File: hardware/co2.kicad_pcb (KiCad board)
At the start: 2 copper layers, 25 x 35 mm, 24 parts, among them P1 CON-SENSOR, U1 M24C64, U2 TLV271, U3 MSH-Sensor, U4 DRILL, U5 DRILL, U6 DRILL, U7 DRILL

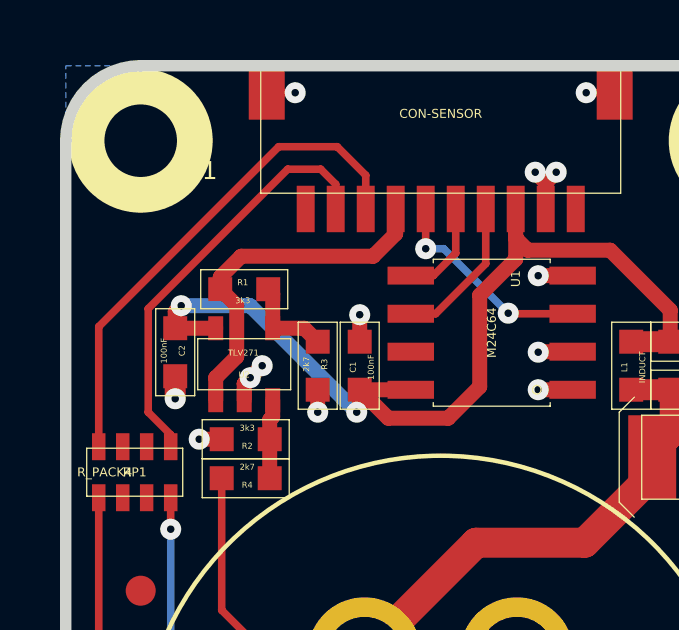
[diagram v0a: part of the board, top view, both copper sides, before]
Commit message: add configurable pin for co2 sensor config
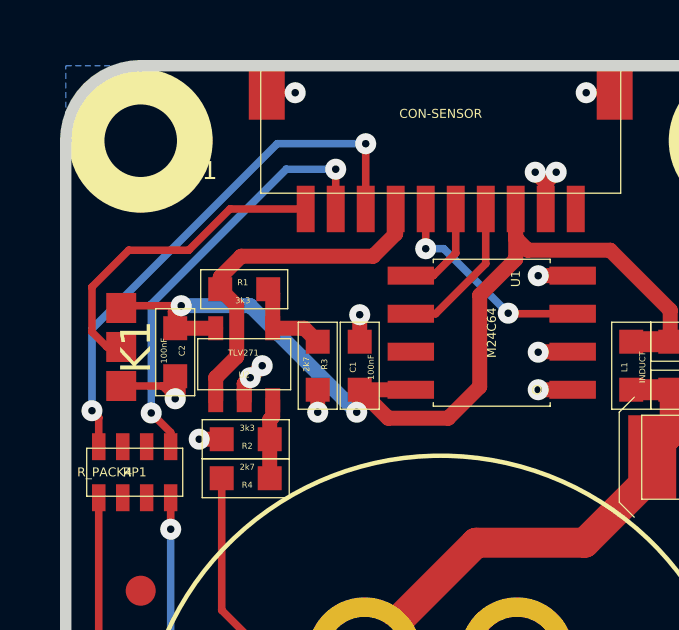
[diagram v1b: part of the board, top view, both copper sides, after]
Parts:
- added K1: CONN_3, kicad-libraries:con-conf, F.Cu at (133.2, 77.5)
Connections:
- P1 pad 10: (no net) -> Net-(K1-Pad2)
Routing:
- net Net-(K1-Pad2): track 0.00 -> 10.9 mm
- net 3V3: track 31.8 -> 33.9 mm
- net GND: track 22.1 -> 24.1 mm
- net Net-(P1-Pad8): track 16.9 -> 17.9 mm, vias 0 -> 2
- net Net-(P1-Pad9): track 14.1 -> 14.4 mm, vias 0 -> 2

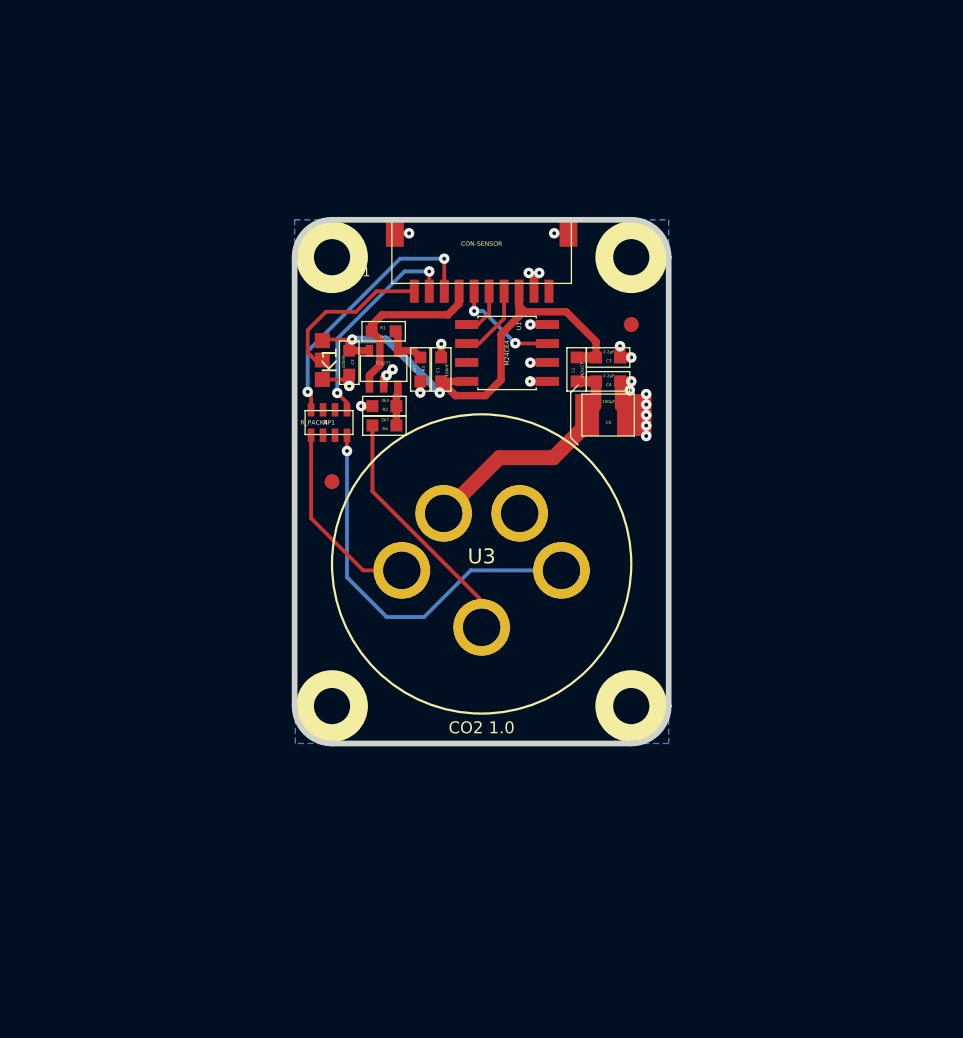
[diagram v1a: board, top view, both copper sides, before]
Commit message: new co2 prototype with k30 sensor
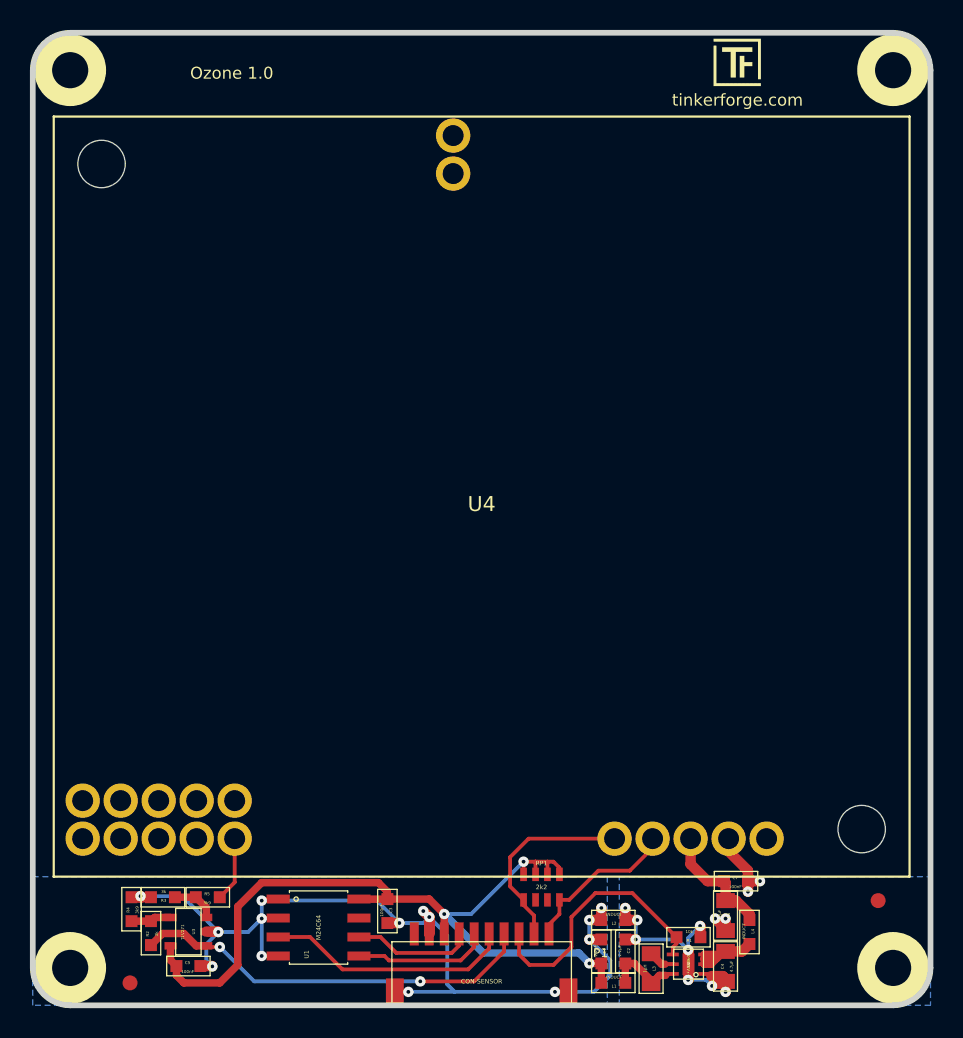
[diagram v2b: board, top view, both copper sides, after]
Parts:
- removed K1: CONN_3, kicad-libraries:con-conf
- added C6: 4.7µF, kicad-libraries:0805, F.Cu at (160.2, 114.6)
- added C7: 100nF, kicad-libraries:0603, F.Cu at (160.9, 112.3)
- added L2: INDUCT, kicad-libraries:0603, F.Cu at (152.7, 114.9)
- added L3: 1µH, kicad-libraries:0805, F.Cu at (155.2, 118.2)
- added L4: INDUCT, kicad-libraries:0603, F.Cu at (161.8, 115.7)
- added R5: 3k9, kicad-libraries:0603, F.Cu at (125.6, 113.4)
- added U8: DRILL, kicad-libraries:DRILL_NP, F.Cu at (116.4, 58.1)
- C1, C2: value 100nF -> 2.2µF
- C3: value 2.2µF -> 100nF
- C4: value 2.2µF -> 4.7µF; footprint kicad-libraries:0603 -> kicad-libraries:0805
- C5: value 100µF -> 100nF; footprint kicad-libraries:3528-21 -> kicad-libraries:0603
- G***: moved to F.Cu
- R1: value 3k3 -> 10k
- R2: value 3k3 -> 3k
- R3: value 2k7 -> 3k
- R4: value 2k7 -> 3k9
- RP1: value R_PACK4 -> 2k2; footprint kicad-libraries:0603X4 -> kicad-libraries:4X0603
- U2: value TLV271 -> FAN4860; footprint kicad-libraries:SOT23-5 -> kicad-libraries:UMLP_22
- U3: value MSH-Sensor -> TLV271; footprint kicad-libraries:MSH-Sensor -> kicad-libraries:SOT23-5
- U4: value DRILL -> K30; footprint kicad-libraries:DRILL_NP -> kicad-libraries:K30
- moved Fiducial_Mark 55.3 mm to (120.4, 119.1)
- moved P1 52.5 mm to (143.9, 120.6), turned to 0 degrees
- moved U5 50.6 mm to (171.4, 118.1)
- moved U6 50.6 mm to (116.4, 118.1)
- moved C5 46.3 mm to (124.3, 118.0), turned to 180 degrees
- moved Fiducial_Mark 46.0 mm to (170.4, 113.6)
- moved U7 46.0 mm to (171.4, 58.1)
- moved R1 45.3 mm to (157.7, 116.0), turned to 0 degrees
- moved U2 44.7 mm to (157.7, 117.8), turned to 270 degrees
- moved G*** 43.8 mm to (159.4, 56.0), turned to 0 degrees
- moved C2 43.5 mm to (153.5, 117.0)
- moved L1 41.1 mm to (152.7, 119.1), turned to 0 degrees
- moved U1 40.4 mm to (133.0, 115.4), turned to 270 degrees
- moved C1 40.3 mm to (151.9, 117.0), turned to 90 degrees
- moved C4 39.9 mm to (160.2, 118.0), turned to 270 degrees
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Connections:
- C1 pad 1: GND -> 3V3
- C1 pad 2: 3V3 -> GND
- C2 pad 1: GND -> Net-(C2-Pad1)
- C2 pad 2: 3V3 -> AGND
- C3 pad 1: 3V3 -> GND
- C3 pad 2: GND -> 3V3
- C4 pad 2: GND -> AGND
- C5 pad 1: Net-(C4-Pad1) -> GND
- C5 pad 2: GND -> 3V3
- L1 pad 2: Net-(C4-Pad1) -> Net-(C2-Pad1)
- P1 pad 10: Net-(K1-Pad2) -> SCL
- P1 pad 8: Net-(P1-Pad8) -> EN
- P1 pad 9: Net-(P1-Pad9) -> SDA
- R1 pad 1: Net-(R1-Pad1) -> EN
- R1 pad 2: Net-(P1-Pad7) -> AGND
- R2 pad 1: GND -> Net-(R2-Pad1)
- R2 pad 2: Net-(R2-Pad2) -> Net-(P1-Pad7)
- R3 pad 2: Net-(R1-Pad1) -> Net-(R3-Pad2)
- R4 pad 1: OUT -> GND
- R4 pad 2: Net-(R2-Pad2) -> Net-(R2-Pad1)
- RP1 pad 1: RX -> 3V3
- RP1 pad 2: (no net) -> 3V3
- RP1 pad 3: (no net) -> 3V3
- RP1 pad 4: TX -> 3V3
- RP1 pad 5: Net-(P1-Pad9) -> SCL
- RP1 pad 8: Net-(P1-Pad8) -> SDA
- U2 pad 1: Net-(P1-Pad7) -> AGND
- U2 pad 2: GND -> Net-(C4-Pad1)
- U2 pad 3: Net-(R2-Pad2) -> Net-(C4-Pad1)
- U2 pad 4: Net-(R1-Pad1) -> EN
- U2 pad 5: 3V3 -> Net-(L3-Pad2)
- U3 pad 1: Net-(C4-Pad1) -> Net-(P1-Pad7)
- U3 pad 2: RX -> GND
- U3 pad 3: OUT -> Net-(R3-Pad2)
- U3 pad 4: TX -> Net-(R2-Pad1)
- U3 pad 5: GND -> 3V3
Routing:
- net GND: track 24.1 -> 66.1 mm, vias 22 -> 14
- net TX: track 26.2 -> 0.00 mm, vias 1 -> 0
- net AGND: track 0.00 -> 24.3 mm, vias 0 -> 12
- net 3V3: track 33.9 -> 55.4 mm, vias 2 -> 3
- net Net-(P1-Pad8): track 17.9 -> 0.00 mm, vias 2 -> 0
- net EN: track 0.00 -> 17.8 mm
- net OUT: track 16.5 -> 0.00 mm
- net Net-(P1-Pad7): track 12.6 -> 27.3 mm, vias 0 -> 2
- net Net-(P1-Pad9): track 14.4 -> 0.00 mm, vias 2 -> 0
- net RX: track 14.0 -> 0.00 mm
- net SDA: track 0.00 -> 13.3 mm
- net Net-(K1-Pad2): track 10.9 -> 0.00 mm
- net SCL: track 0.00 -> 10.8 mm
- net Net-(P1-Pad6): track 7.12 -> 16.6 mm, vias 2 -> 0
- net Net-(C4-Pad1): track 16.5 -> 7.64 mm
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- added copper zone on B.Cu, net AGND
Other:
- board size 25 x 35 mm -> 60 x 65 mm
- board text added: "Ozone 1.0"
- board text removed: "CO2 1.0"

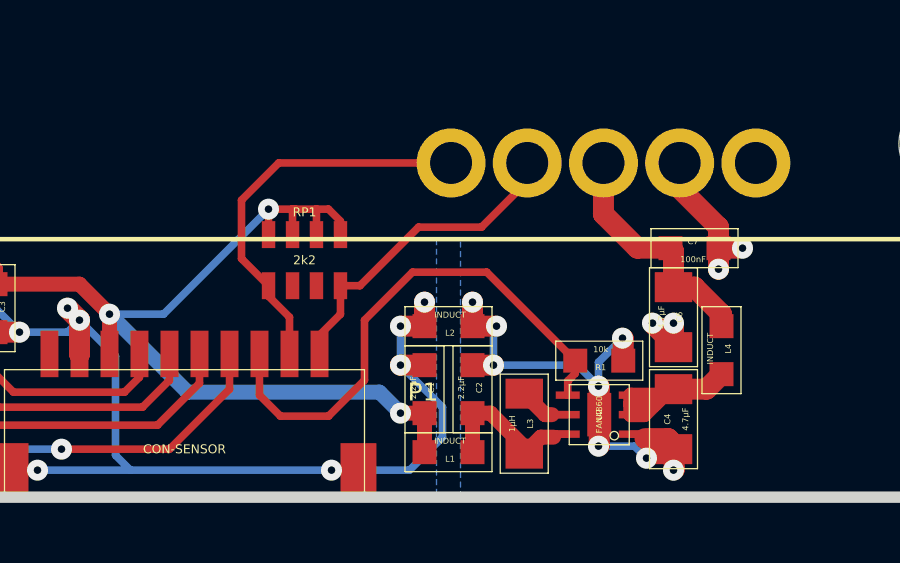
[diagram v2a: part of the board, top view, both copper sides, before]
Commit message: change gnd inductor to 0 ohm resistor
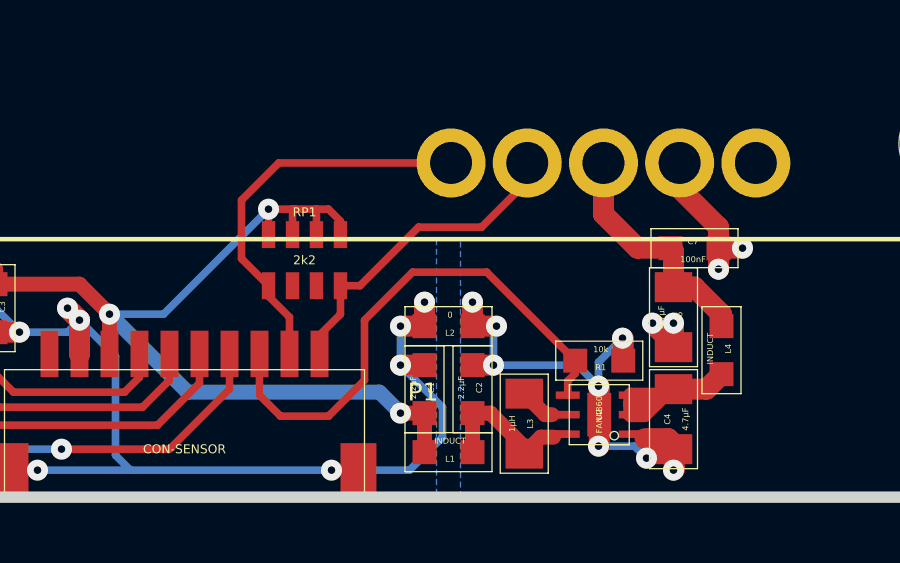
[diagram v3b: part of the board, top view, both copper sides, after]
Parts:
- L2: value INDUCT -> 0

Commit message: fix product name
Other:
- board text added: "CO2 1.0"
- board text removed: "Ozone 1.0"
